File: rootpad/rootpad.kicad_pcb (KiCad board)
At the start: 2 copper layers, 52 parts, among them J1 USB_B_Mini, SW1 SW_Push, U1 ATmega32U4-AU, Y1 16MHz

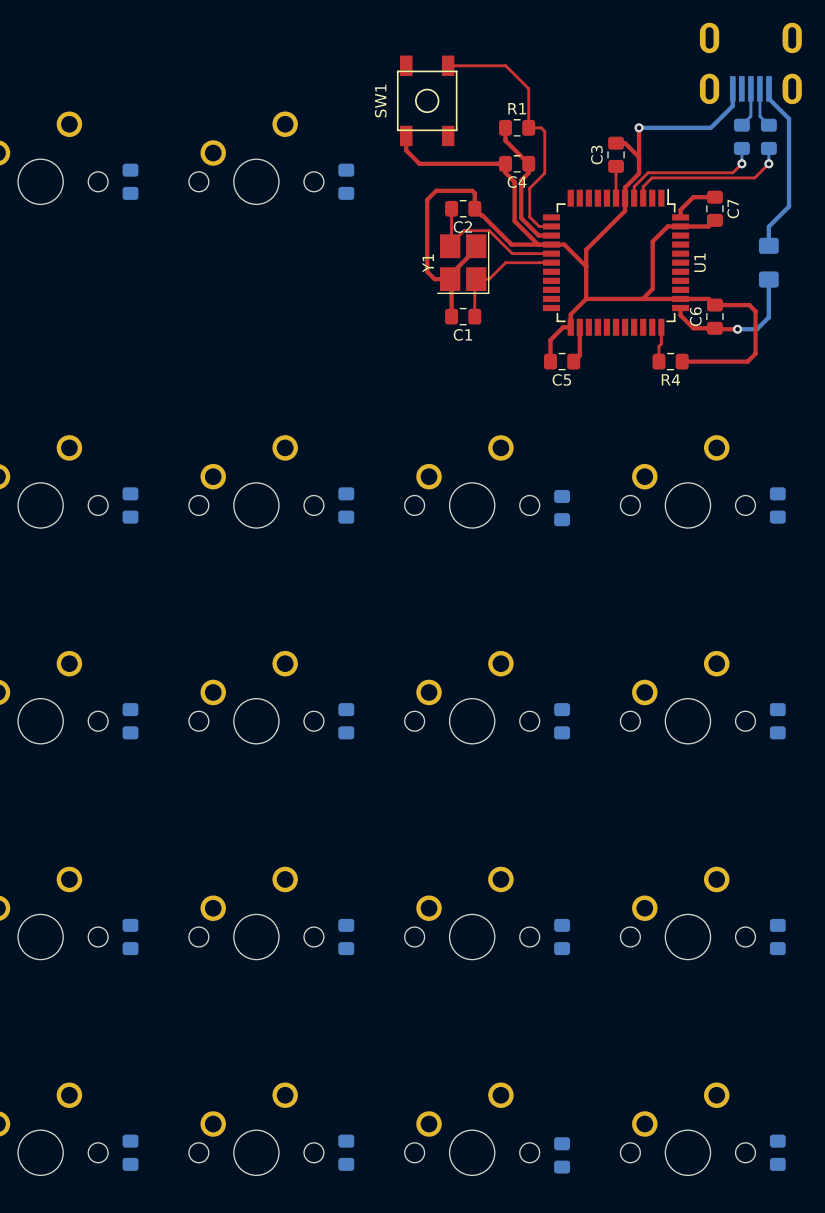
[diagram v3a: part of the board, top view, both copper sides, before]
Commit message: Finished route of mcu
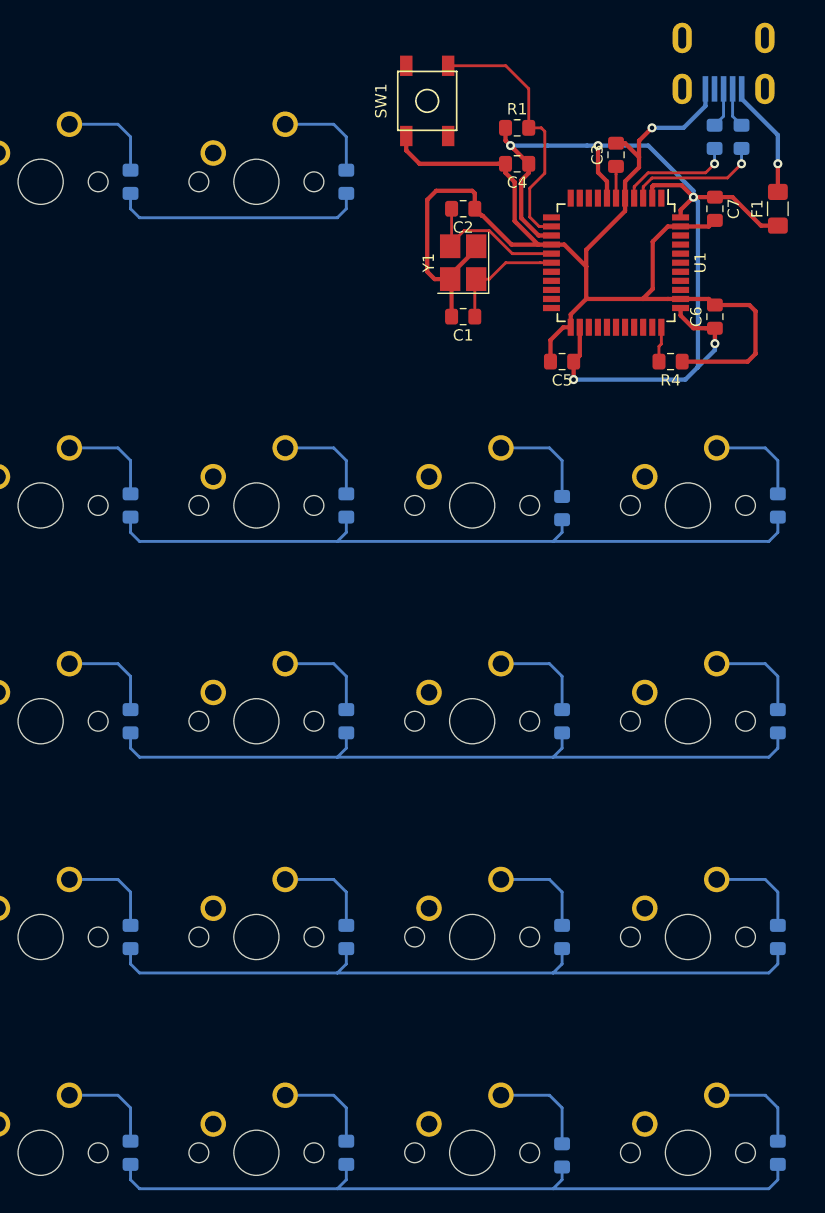
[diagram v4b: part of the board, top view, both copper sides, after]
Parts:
- F1: moved to F.Cu
- moved F1 4.83 mm to (193.7, 59.5)
- moved R2 2.41 mm to (188.1, 53.2)
- moved J1 2.41 mm to (188.9, 44.5)
- moved R3 2.41 mm to (190.5, 53.2)
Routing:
- net ROW3: track 0.00 -> 65.5 mm
- net ROW2: track 0.00 -> 65.5 mm
- net ROW4: track 0.00 -> 65.2 mm
- net ROW1: track 0.00 -> 65.2 mm
- net +5V: track 32.5 -> 91.9 mm, vias 1 -> 5
- net ROW0: track 0.00 -> 22.4 mm
- net Net-(D17-Pad2): track 0.00 -> 9.03 mm
- net Net-(D5-Pad2): track 0.00 -> 9.03 mm
- net Net-(D6-Pad2): track 0.00 -> 8.80 mm
- net Net-(D3-Pad2): track 0.00 -> 8.80 mm
- net Net-(D9-Pad2): track 0.00 -> 8.80 mm
- net Net-(D7-Pad2): track 0.00 -> 8.80 mm
- net Net-(D18-Pad2): track 0.00 -> 8.80 mm
- net Net-(D15-Pad2): track 0.00 -> 8.80 mm
- net Net-(D10-Pad2): track 0.00 -> 8.80 mm
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
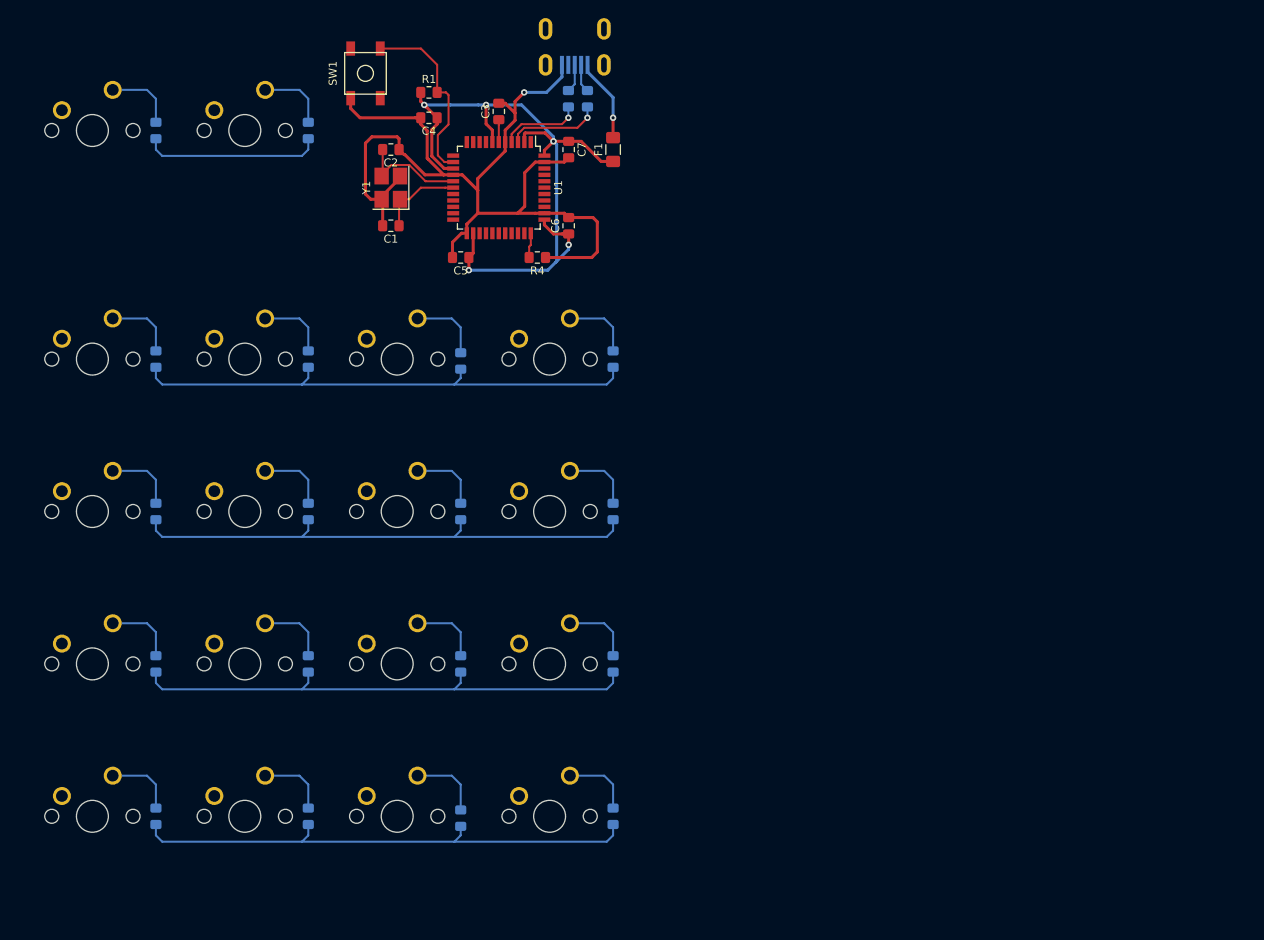
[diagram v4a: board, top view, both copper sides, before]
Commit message: Initial route of matrix. Not connected
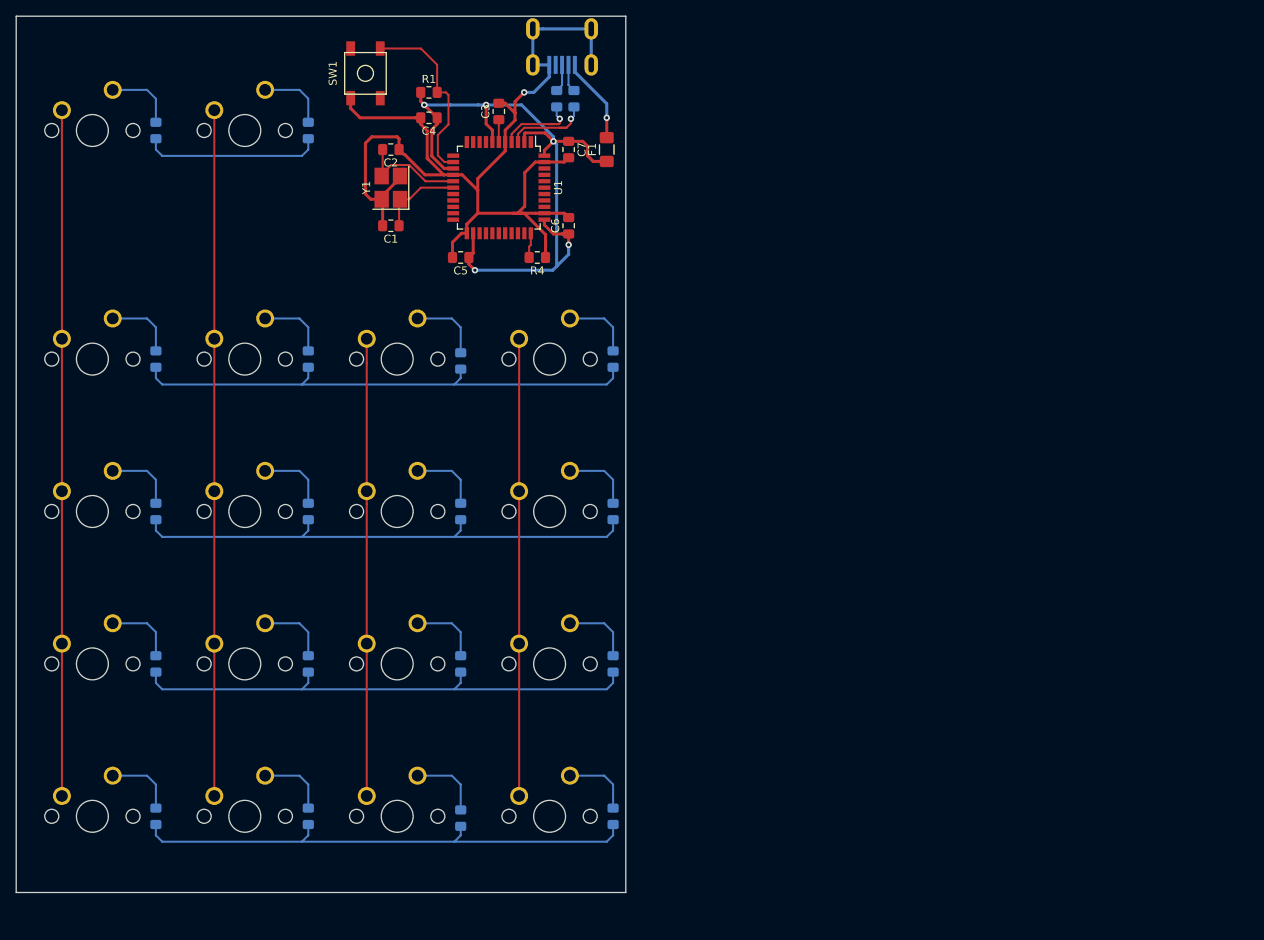
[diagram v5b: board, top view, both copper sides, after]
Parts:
- moved R3 1.68 mm to (188.8, 53.2)
- moved J1 1.59 mm to (187.3, 44.5)
- moved R2 1.46 mm to (186.6, 53.2)
- moved F1 0.79 mm to (192.9, 59.5)
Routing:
- net COL1: track 0.00 -> 85.7 mm
- net COL0: track 0.00 -> 85.7 mm
- net COL3: track 0.00 -> 57.2 mm
- net COL2: track 0.00 -> 57.2 mm
- net GND: track 125.2 -> 136.1 mm
- net Net-(R3-Pad2): track 11.9 -> 11.3 mm
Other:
- board outline added: 76.2 x 109.5 mm

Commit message: Finished connection matrix to mcu
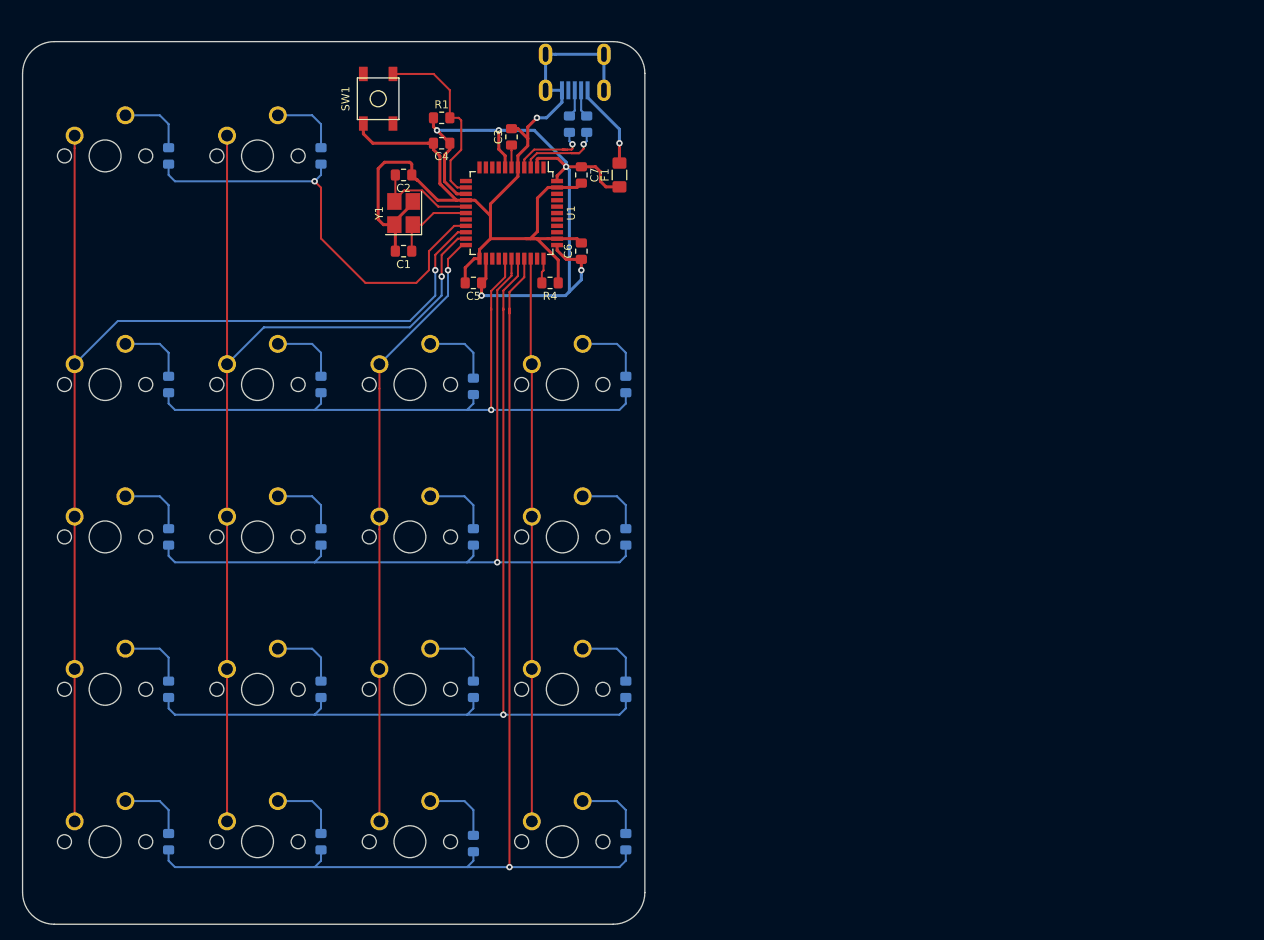
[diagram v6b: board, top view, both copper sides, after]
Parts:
- moved D17 3.55 mm to (176.2, 146.3)
- moved C3 3.55 mm to (181.0, 57.9)
- moved C4 3.55 mm to (172.2, 58.7)
- moved D12 3.55 mm to (157.2, 127.0)
- moved D13 3.55 mm to (176.2, 127.0)
- moved D2 3.55 mm to (157.2, 60.3)
- moved D4 3.55 mm to (157.2, 88.9)
- moved D5 3.55 mm to (176.2, 89.1)
- moved F1 3.55 mm to (194.5, 62.7)
- moved MX12 3.55 mm to (149.2, 127.0)
- moved MX13 3.55 mm to (168.3, 127.0)
- moved MX2 3.55 mm to (149.2, 60.3)
- moved MX4 3.55 mm to (149.2, 88.9)
- moved MX5 3.55 mm to (168.3, 88.9)
- moved R2 3.55 mm to (188.2, 56.4)
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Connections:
- U1 pad 19: Net-(U1-Pad19) -> ROW0
- U1 pad 20: Net-(U1-Pad20) -> COL0
- U1 pad 21: Net-(U1-Pad21) -> COL1
- U1 pad 22: Net-(U1-Pad22) -> COL2
- U1 pad 27: Net-(U1-Pad27) -> ROW1
- U1 pad 28: Net-(U1-Pad28) -> ROW2
- U1 pad 29: Net-(U1-Pad29) -> ROW3
- U1 pad 30: Net-(U1-Pad30) -> ROW4
- U1 pad 31: Net-(U1-Pad31) -> COL3
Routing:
- net ROW4: track 65.2 -> 142.7 mm, vias 0 -> 1
- net COL0: track 85.7 -> 144.5 mm, vias 0 -> 1
- net ROW3: track 65.5 -> 123.4 mm, vias 0 -> 1
- net COL1: track 85.7 -> 125.1 mm, vias 0 -> 1
- net ROW2: track 65.5 -> 104.2 mm, vias 0 -> 1
- net ROW0: track 22.4 -> 54.7 mm, vias 0 -> 1
- net ROW1: track 65.2 -> 85.1 mm, vias 0 -> 1
- net COL2: track 57.2 -> 76.8 mm, vias 0 -> 1
- net COL3: track 57.2 -> 70.4 mm
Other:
- board size 76.2 x 109.5 mm -> 77.8 x 110.3 mm

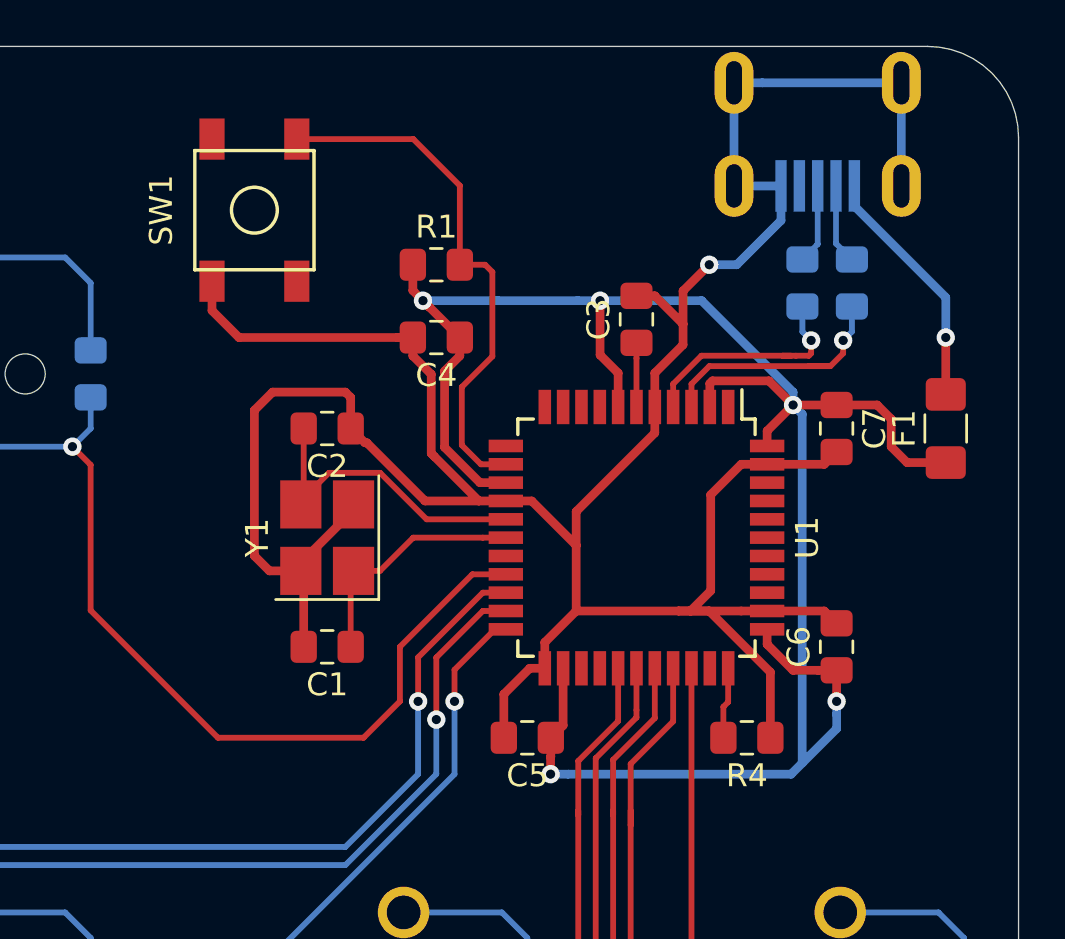
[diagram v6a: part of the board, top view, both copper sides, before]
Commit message: Added and routed LED
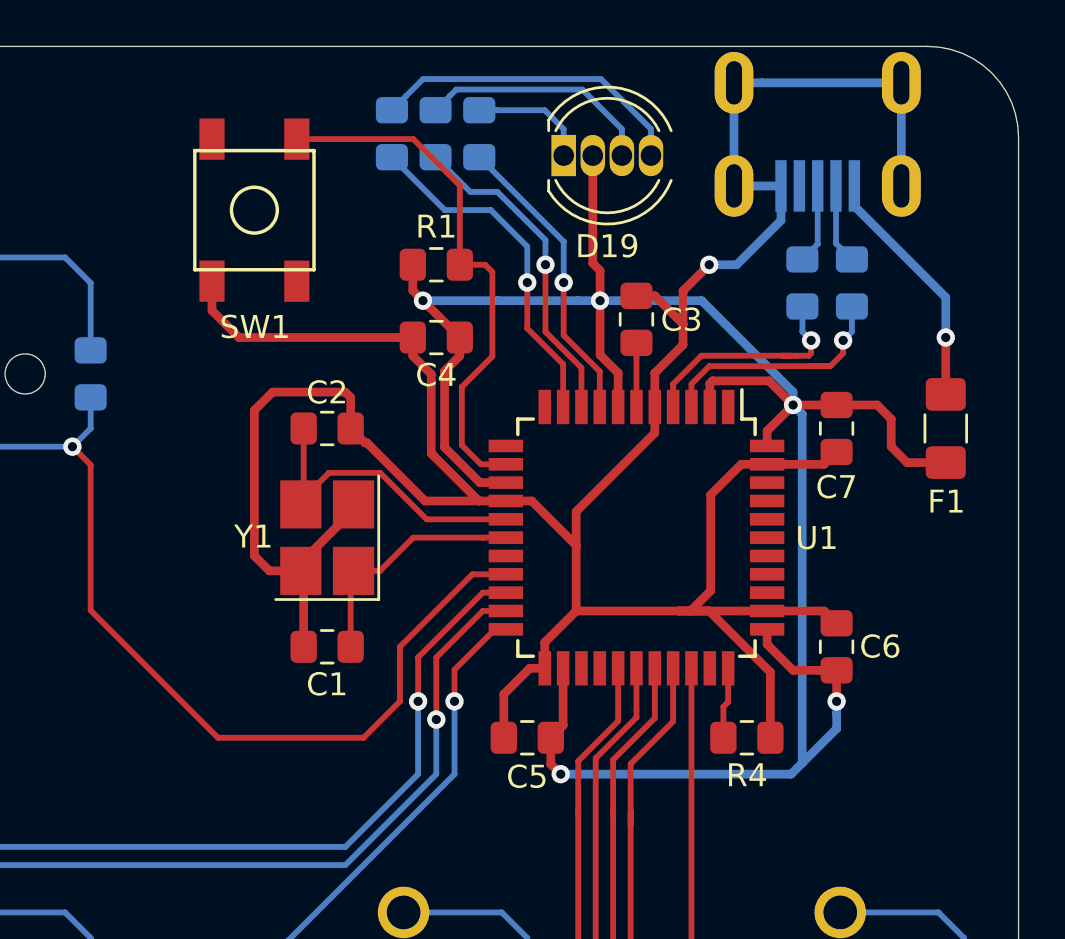
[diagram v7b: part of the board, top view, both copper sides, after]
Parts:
- added D19: LED_RAGB, LED_THT:LED_D5.0mm-4_RGB, F.Cu at (177.8, 50.8)
- added R5: 150, Resistor_SMD:R_0805_2012Metric_Pad1.15x1.40mm_HandSolder, B.Cu at (174.1, 49.8)
- added R6: 80, Resistor_SMD:R_0805_2012Metric_Pad1.15x1.40mm_HandSolder, B.Cu at (172.2, 49.8)
- added R7: 80, Resistor_SMD:R_0805_2012Metric_Pad1.15x1.40mm_HandSolder, B.Cu at (170.3, 49.8)
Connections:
- U1 pad 10: Net-(U1-Pad10) -> LED_B
- U1 pad 8: Net-(U1-Pad8) -> LED_R
- U1 pad 9: Net-(U1-Pad9) -> LED_G
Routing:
- net LED_B: track 0.00 -> 15.2 mm, vias 0 -> 1
- net LED_G: track 0.00 -> 14.2 mm, vias 0 -> 1
- net Net-(D19-Pad4): track 0.00 -> 13.9 mm
- net LED_R: track 0.00 -> 13.1 mm, vias 0 -> 1
- net Net-(D19-Pad3): track 0.00 -> 10.4 mm
- net +5V: track 92.7 -> 98.9 mm
- net Net-(D19-Pad1): track 0.00 -> 5.18 mm

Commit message: Completed routing and prettied up board
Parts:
- D1, D10, D11, D12, D13, D14, D15, D16, D17, D18, D2, D3, D4, D5, D6, D7, D8, D9: footprint Diode_SMD:D_0805_2012Metric_Pad1.15x1.40mm_HandSolder -> Diode_THT:D_DO-35_SOD27_P7.62mm_Horizontal
- SW1: footprint random-keyboard-parts:SKQG-1155865 -> Button_Switch_SMD:SW_Push_1P1T_NO_6x6mm_H9.5mm
- moved SW1 4.63 mm to (168.3, 50.8), turned to 180 degrees
- moved D11 3.98 mm to (138.4, 131.0)
- moved D15 3.98 mm to (138.4, 150.0)
- moved D3 3.98 mm to (138.4, 92.9)
- moved D7 3.98 mm to (138.4, 111.9)
- moved D10 3.98 mm to (195.6, 111.9)
- moved D12 3.98 mm to (157.5, 131.0)
- moved D13 3.98 mm to (176.5, 131.0)
- moved D14 3.98 mm to (195.6, 131.0)
- moved D16 3.98 mm to (157.5, 150.0)
- moved D18 3.98 mm to (195.6, 150.0)
- moved D4 3.98 mm to (157.5, 92.9)
- moved D6 3.98 mm to (195.6, 92.9)
- moved D8 3.98 mm to (157.5, 111.9)
- moved D9 3.98 mm to (176.5, 111.9)
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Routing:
- net GND: track 136.1 -> 149.5 mm, vias 1 -> 3
- net ROW1: track 85.1 -> 79.2 mm, vias 1 -> 0
- net ROW2: track 104.2 -> 98.8 mm, vias 1 -> 0
- net ROW0: track 54.7 -> 50.0 mm, vias 1 -> 0
- net ROW3: track 123.4 -> 118.9 mm, vias 1 -> 0
- net Net-(R1-Pad2): track 23.3 -> 27.8 mm
- net ROW4: track 142.7 -> 139.1 mm, vias 1 -> 0
- net Net-(D17-Pad2): track 9.03 -> 6.31 mm
- net Net-(D5-Pad2): track 9.03 -> 6.31 mm
- net Net-(D16-Pad2): track 8.80 -> 6.31 mm
- net Net-(D18-Pad2): track 8.80 -> 6.31 mm
- net Net-(D9-Pad2): track 8.80 -> 6.31 mm
- net Net-(D8-Pad2): track 8.80 -> 6.31 mm
- net Net-(D6-Pad2): track 8.80 -> 6.31 mm
- net Net-(D4-Pad2): track 8.80 -> 6.31 mm
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- added copper zone on B.Cu, net GND
- added copper zone on F.Cu, net GND
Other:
- board text added: "\///\//\`/"
